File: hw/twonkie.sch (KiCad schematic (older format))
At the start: 54 parts, among them J1 USB_C_Plug, J2 USB_C_Receptacle, J3 USB_B_Micro, Q1 BSD840N, Q2 BSD840N, Q3 BSD840N, SW1 TACT, U1 AD8620, U2 AD8620, U3 AD8620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

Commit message: Half a PCB - USB-C side laid out
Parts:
- removed NT1: Net-Tie_2, symbol Device:Net-Tie_2
- added C9: 100n, Capacitor_SMD:C_0402_1005Metric_Pad0.74x0.62mm_HandSolder, symbol Device:C
- C1, C2, C3, C8: footprint (none) -> Capacitor_SMD:C_0402_1005Metric_Pad0.74x0.62mm_HandSolder
- C4: renamed from C6; footprint (none) -> Capacitor_SMD:C_0402_1005Metric_Pad0.74x0.62mm_HandSolder
- C5: renamed from C4; footprint (none) -> Capacitor_SMD:C_0402_1005Metric_Pad0.74x0.62mm_HandSolder
- C6: renamed from C7; footprint (none) -> Capacitor_SMD:C_0402_1005Metric_Pad0.74x0.62mm_HandSolder
- C7: renamed from C5; footprint (none) -> Capacitor_SMD:C_0402_1005Metric_Pad0.74x0.62mm_HandSolder
- DS1, DS2: footprint (none) -> LED_SMD:LED_Cree-PLCC4_3.2x2.8mm_CCW
- FB1: renamed from FB2; footprint (none) -> Inductor_SMD:L_0402_1005Metric_Pad0.77x0.64mm_HandSolder
- FB2: renamed from FB1; footprint (none) -> Inductor_SMD:L_0402_1005Metric_Pad0.77x0.64mm_HandSolder
- J1: footprint (none) -> twonkie:JAE_DX07P024AJ1R1500; symbol Connector:USB_C_Plug -> twonkie:USB_C_Plug
- J2: footprint (none) -> twonkie:EDAC_690-024-294T331_EdgeMount; symbol Connector:USB_C_Receptacle -> twonkie:USB_C_Receptacle
- J3: footprint (none) -> Connector_USB:USB_Micro-B_Wuerth_629105150521_CircularHoles
- R1, R14, R15, R16, R17, R18, R19, R2, R20, R21, R22, R23, R3: footprint (none) -> Resistor_SMD:R_0402_1005Metric_Pad0.72x0.64mm_HandSolder
- R10: renamed from R7; footprint (none) -> Resistor_SMD:R_0402_1005Metric_Pad0.72x0.64mm_HandSolder
- R11: renamed from R8; footprint (none) -> Resistor_SMD:R_0402_1005Metric_Pad0.72x0.64mm_HandSolder
- R12: renamed from R10; footprint (none) -> Resistor_SMD:R_0402_1005Metric_Pad0.72x0.64mm_HandSolder
- R13: renamed from R11; footprint (none) -> Resistor_SMD:R_0402_1005Metric_Pad0.72x0.64mm_HandSolder
- R4: renamed from R5; footprint (none) -> Resistor_SMD:R_0402_1005Metric_Pad0.72x0.64mm_HandSolder
- R5: renamed from R9; footprint (none) -> Resistor_SMD:R_0402_1005Metric_Pad0.72x0.64mm_HandSolder
- R6: renamed from R12; footprint (none) -> Resistor_SMD:R_0402_1005Metric_Pad0.72x0.64mm_HandSolder
- R7: renamed from R13; footprint (none) -> Resistor_SMD:R_0402_1005Metric_Pad0.72x0.64mm_HandSolder
- R8: renamed from R4; footprint (none) -> Resistor_SMD:R_0402_1005Metric_Pad0.72x0.64mm_HandSolder
- R9: renamed from R6; footprint (none) -> Resistor_SMD:R_0402_1005Metric_Pad0.72x0.64mm_HandSolder
- SW1: footprint (none) -> Button_Switch_SMD:SW_SPST_Omron_B3FS-100xP
- TP1, TP2, TP3, TP4, TP5: footprint (none) -> TestPoint:TestPoint_Pad_D1.5mm
- U1, U2: value AD8620 -> INA260; footprint (none) -> Package_SO:TSSOP-16_4.4x5mm_P0.65mm
- U3: value AD8620 -> MIC5504; footprint (none) -> Package_TO_SOT_SMD:SOT-23-5_HandSoldering
- U4: footprint (none) -> Package_QFP:LQFP-48_7x7mm_P0.5mm
- U5: footprint (none) -> Package_SO:MSOP-8_3x3mm_P0.65mm
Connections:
- net labels added: CC2_PLUG, RX1+, RX1-, RX2+, RX2-, SBU1, SBU2, TX1+, TX1-, TX2+, TX2-, TX_CLK, USBC_D+, USBC_D-, USB_B_D+, USB_B_D-, VBUS_PLUG, VBUS_RECEP
- net labels removed: TX_CLKIN, TX_CLKOUT, USB_B_DM, USB_B_DP
- wire segments 204 -> 203
- no-connect marks 5 -> 8
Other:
- note removed: "This space for rent"
- moved on the sheet: U1, U2

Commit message: Ratsnest Zero \o/
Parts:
- SW1: footprint Button_Switch_SMD:SW_SPST_Omron_B3FS-100xP -> Button_Switch_SMD:SW_SPST_EVQP7C; symbol Switch:SW_MEC_5E -> Switch:SW_Push
- TP1, TP2, TP3, TP4, TP5: footprint TestPoint:TestPoint_Pad_D1.5mm -> TestPoint:TestPoint_Pad_D1.0mm
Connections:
- net PB10 is gone; now on net LED_G_L: U4.21 (PB10)
- net PB12 is gone; now on net CC2_RPUSB: U4.25 (PB12)
- net PC13 is gone; now on net CC2_TX_EN: U4.2 (PC13)
- net BOOT: now also SW1.2; no longer SW1.3 (K), SW1.4 (A)
- net CC1_RA: now also U4.39 (PB3); no longer U4.29 (PA8)
- net CC1_RD: now also U4.40 (PB4); no longer U4.41 (PB5)
- net CC1_RP1A5: now also U4.45 (PB8); no longer U4.37 (PA14)
- net CC1_RP3A0: now also U4.41 (PB5); no longer U4.38 (PA15)
- net CC1_RPUSB: now also U4.3 (PC14); no longer U4.34 (PA13)
- net CC1_TX_DATA: now also U4.38 (PA15); no longer U4.40 (PB4)
- net CC1_TX_EN: now also U4.37 (PA14); no longer U4.19 (PB1)
- net CC2_RA: now also U4.34 (PA13); no longer U4.28 (PB15)
- net CC2_RD: now also U4.29 (PA8); no longer U4.45 (PB8)
- net CC2_RP1A5: now also U4.26 (PB13); no longer U4.3 (PC14)
- net CC2_RP3A0: now also U4.28 (PB15); no longer U4.4 (PC15)
- net CC2_RPUSB: no longer U4.18 (PB0)
- net CC2_TX_DATA: now also U4.4 (PC15); no longer U4.16 (PA6)
- net CC2_TX_EN: no longer U4.39 (PB3)
- net GND: no longer SW1.2
- net LED_G_L: no longer U4.22 (PB11)
- net LED_R_L: now also U4.22 (PB11); no longer U4.26 (PB13)
- no-connect marks 8 -> 5
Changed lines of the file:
@@
 $EndComp
 $Comp
-L Switch:SW_MEC_5E SW1
+L Switch:SW_Push SW1
 U 1 1 5FAB092D
-P 7700 3300
-F 0 "SW1" H 7700 3685 50  0000 C CNN
-F 1 "TACT" H 7700 3594 50  0000 C CNN
-F 2 "Button_Switch_SMD:SW_SPST_Omron_B3FS-100xP" H 7700 3600 50  0001 C CNN
-F 3 "http://www.apem.com/int/index.php?controller=attachment&id_attachment=1371" H 7700 3600 50  0001 C CNN
-	1    7700 3300
+P 7500 3200
+F 0 "SW1" H 7500 3400 50  0000 C CNN
+F 1 "TACT" H 7500 3100 50  0000 C CNN
+F 2 "Button_Switch_SMD:SW_SPST_EVQP7C" H 7500 3500 50  0001 C CNN
+F 3 "http://www.apem.com/int/index.php?controller=attachment&id_attachment=1371" H 7500 3500 50  0001 C CNN
+	1    7500 3200
 	-1   0    0    -1
 $EndComp
@@
 Wire Wire Line
 	7500 4850 8400 4850
-Text Label 7500 4550 0    50   ~ 0
+Text Label 7500 5750 0    50   ~ 0
 CC2_RPUSB
-Text Label 7500 4650 0    50   ~ 0
+Text Label 10500 5950 2    50   ~ 0
 CC1_TX_EN
 Text Label 7500 4750 0    50   ~ 0
 VBUS_ALERT_L
-Text Label 7500 4850 0    50   ~ 0
+Text Label 7500 4150 0    50   ~ 0
 CC2_TX_EN
 Wire Wire Line
@@
 Wire Wire Line
 	7500 5250 8400 5250
+Text Label 10500 6050 2    50   ~ 0
+CC1_TX_DATA
 Text Label 7500 4950 0    50   ~ 0
-CC1_TX_DATA
-Text Label 7500 5050 0    50   ~ 0
 CC1_RD
 Text Label 7500 5150 0    50   ~ 0
@@
 Wire Wire Line
 	7500 5650 8400 5650
-Text Label 7500 5350 0    50   ~ 0
+Text Label 10500 5350 2    50   ~ 0
 CC2_RD
 Text Label 7500 5450 0    50   ~ 0
 TX_CLK
 Text Label 7500 5650 0    50   ~ 0
-LED_G_L
+LED_R_L
 Wire Wire Line
 	7500 5850 8400 5850
@@
 Wire Wire Line
 	7500 6050 8400 6050
-Text Label 7500 5850 0    50   ~ 0
-LED_R_L
 Text Label 7500 5950 0    50   ~ 0
 LED_B_L
-Text Label 7500 6050 0    50   ~ 0
+Text Label 10500 5850 2    50   ~ 0
 CC2_RA
 Wire Wire Line
@@
 Text Label 10500 5050 2    50   ~ 0
 TX_CLK
-Text Label 10500 5150 2    50   ~ 0
+Text Label 7500 4350 0    50   ~ 0
 CC2_TX_DATA
 Text Label 10500 5250 2    50   ~ 0
@@
 Wire Wire Line
 	10500 5650 9600 5650
-Text Label 10500 5350 2    50   ~ 0
+Text Label 7500 4850 0    50   ~ 0
 CC1_RA
 Text Label 10500 5450 2    50   ~ 0
@@
 Text Label 10500 5750 2    50   ~ 0
 USB_B_D+
-Text Label 10500 5850 2    50   ~ 0
-CC1_RPUSB
-Text Label 10500 5950 2    50   ~ 0
+Text Label 7500 5350 0    50   ~ 0
 CC1_RP1A5
-Text Label 10500 6050 2    50   ~ 0
+Text Label 7500 5050 0    50   ~ 0
 CC1_RP3A0
 Wire Wire Line
@@
 F 0 "TP5" V 7500 3800 50  0000 C CNN
 F 1 "TestPoint" V 7604 3622 50  0001 C CNN
-F 2 "TestPoint:TestPoint_Pad_D1.5mm" H 7700 3550 50  0001 C CNN
+F 2 "TestPoint:TestPoint_Pad_D1.0mm" H 7700 3550 50  0001 C CNN
 F 3 "~" H 7700 3550 50  0001 C CNN
 	1    7500 3550
 	0    -1   -1   0
 $EndComp
-Wire Wire Line
-	7500 3300 7500 3200
-Connection ~ 7500 3200
-Wire Wire Line
-	7900 3300 7900 3200
 $Comp
 L power:GND #PWR0124
 U 1 1 5FE51FD2
-P 7900 3300
-F 0 "#PWR0124" H 7900 3050 50  0001 C CNN
-F 1 "GND" H 7905 3127 50  0000 C CNN
-F 2 "" H 7900 3300 50  0001 C CNN
-F 3 "" H 7900 3300 50  0001 C CNN
-	1    7900 3300
+P 7700 3200
+F 0 "#PWR0124" H 7700 2950 50  0001 C CNN
+F 1 "GND" H 7705 3027 50  0000 C CNN
+F 2 "" H 7700 3200 50  0001 C CNN
+F 3 "" H 7700 3200 50  0001 C CNN
+	1    7700 3200
 	-1   0    0    -1
 $EndComp
-Connection ~ 7900 3300
 Wire Wire Line
 	7100 3950 8400 3950
 Wire Wire Line
-	7500 3200 7100 3200
+	7300 3200 7100 3200
 $Comp
 L power:+3V3 #PWR0125
@@
 F 0 "TP1" V 7500 4000 50  0000 C CNN
 F 1 "TestPoint" V 7604 3822 50  0001 C CNN
-F 2 "TestPoint:TestPoint_Pad_D1.5mm" H 7700 3750 50  0001 C CNN
+F 2 "TestPoint:TestPoint_Pad_D1.0mm" H 7700 3750 50  0001 C CNN
 F 3 "~" H 7700 3750 50  0001 C CNN
 	1    7500 3750
@@
 F 0 "TP2" V 7500 4100 50  0000 C CNN
 F 1 "TestPoint" V 7604 3922 50  0001 C CNN
-F 2 "TestPoint:TestPoint_Pad_D1.5mm" H 7700 3850 50  0001 C CNN
+F 2 "TestPoint:TestPoint_Pad_D1.0mm" H 7700 3850 50  0001 C CNN
 F 3 "~" H 7700 3850 50  0001 C CNN
 	1    7500 3850
@@
 Wire Wire Line
 	8400 4150 7500 4150
-Text Label 7500 4250 0    50   ~ 0
-CC2_RP1A5
-Text Label 7500 4350 0    50   ~ 0
+Text Label 7500 6050 0    50   ~ 0
 CC2_RP3A0
 Wire Wire Line
@@
 Wire Wire Line
 	8400 5750 7500 5750
-Text Label 7500 5750 0    50   ~ 0
-PB12
 Text Label 7500 5550 0    50   ~ 0
-PB10
-Text Label 7500 4150 0    50   ~ 0
-PC13
+LED_G_L
 $Comp
 L Connector:TestPoint TP3
@@
 F 0 "TP3" V 10500 5700 50  0000 C CNN
 F 1 "TestPoint" V 10604 5522 50  0001 C CNN
-F 2 "TestPoint:TestPoint_Pad_D1.5mm" H 10700 5450 50  0001 C CNN
+F 2 "TestPoint:TestPoint_Pad_D1.0mm" H 10700 5450 50  0001 C CNN
 F 3 "~" H 10700 5450 50  0001 C CNN
 	1    10500 5450
@@
 F 0 "TP4" V 10500 5800 50  0000 C CNN
 F 1 "TestPoint" V 10604 5622 50  0001 C CNN
-F 2 "TestPoint:TestPoint_Pad_D1.5mm" H 10700 5550 50  0001 C CNN
+F 2 "TestPoint:TestPoint_Pad_D1.0mm" H 10700 5550 50  0001 C CNN
 F 3 "~" H 10700 5550 50  0001 C CNN
 	1    10500 5550
@@
 	-1   0    0    1
 $EndComp
-NoConn ~ 7500 4150
-NoConn ~ 7500 5550
-NoConn ~ 7500 5750
 NoConn ~ 10500 4950
 NoConn ~ 4600 7300
@@
 	1    0    0    -1
 $EndComp
+Text Label 7500 5850 0    50   ~ 0
+CC2_RP1A5
+Text Label 7500 4250 0    50   ~ 0
+CC1_RPUSB
 $EndSCHEMATC

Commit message: Silk screen, ground plane fixes, move vias out of pads, part numbers
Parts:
- C1, C5: DigiKey P/N (none) -> 1276-1235-1-ND; Manufacturer (none) -> Samsung Electro-Mechanics; Mfg P/N (none) -> CL05A105MQ5NNNC
- C2, C7: DigiKey P/N (none) -> 1276-1481-1-ND; Manufacturer (none) -> Samsung Electro-Mechanics; Mfg P/N (none) -> CL05A475KQ5NRNC
- C3, C4, C8, C9: DigiKey P/N (none) -> 1276-6720-1-ND; Manufacturer (none) -> Samsung Electro-Mechanics; Mfg P/N (none) -> CL05B104KA5NNNC
- C6: DigiKey P/N (none) -> 1276-1028-1-ND; Manufacturer (none) -> Samsung Electro-Mechanics; Mfg P/N (none) -> CL05B103KB5NNNC
- D1: DigiKey P/N (none) -> BZT52C5V6-13-FDICT-ND; Manufacturer (none) -> Diodes Inc.; Mfg P/N (none) -> BZT52C5V6-13-F
- DS1, DS2: value LED_ARBG -> CLVBA-FKA; symbol Device:LED_ARBG -> Device:LED_RABG; DigiKey P/N (none) -> CLVBA-FKA-CAEDH8BBB7A363CT-ND; Manufacturer (none) -> Cree; Mfg P/N (none) -> CLVBA-FKA-CAEDH8BBB7A363
- FB1, FB2: DigiKey P/N (none) -> 490-1006-1-ND; Manufacturer (none) -> MuRata; Mfg P/N (none) -> BLM15AG601SN1D
- J1: value USB_C_Plug -> DX07P024AJ1R1500; DigiKey P/N (none) -> 670-2868-1-ND; Manufacturer (none) -> JAE; Mfg P/N (none) -> DX07P024AJ1R1500
- J2: value USB_C_Receptacle -> 690-024-294T331; DigiKey P/N (none) -> 151-1601-1-ND; Manufacturer (none) -> EDAC; Mfg P/N (none) -> 690-024-294T331
- J3: value USB_B_Micro -> 629105150521; DigiKey P/N (none) -> 732-5960-1-ND; Manufacturer (none) -> Würth; Mfg P/N (none) -> 629105150521
- Q1, Q2, Q3: DigiKey P/N (none) -> BSD840NH6327XTSA1CT-ND; Manufacturer (none) -> Infineon; Mfg P/N (none) -> BSD840NH6327XTSA1
- R1: DigiKey P/N (none) -> 311-51.1KLRCT-ND; Manufacturer (none) -> Yageo; Mfg P/N (none) -> RC0402FR-0751K1L
- R10, R18: Manufacturer (none) -> Yageo; Mfg P/N (none) -> RC0402FR-071KL
- R11, R19: Manufacturer (none) -> Yageo; Mfg P/N (none) -> RC0402FR-0712K1L
- R12, R20: Manufacturer (none) -> Yageo; Mfg P/N (none) -> RC0402FR-075K11L
- R13, R21: Manufacturer (none) -> Yageo; Mfg P/N (none) -> RC0402FR-0735K7L
- R14, R22: Manufacturer (none) -> Yageo; Mfg P/N (none) -> RC0402FR-07200RL
- R15, R23: Manufacturer (none) -> Yageo; Mfg P/N (none) -> RC0402FR-07100RL
- R16, R8: DigiKey P/N (none) -> 311-301KLRCT-ND; Manufacturer (none) -> Yageo; Mfg P/N (none) -> RC0402FR-07301KL
- R17, R9: DigiKey P/N (none) -> 311-4.75KLCT-ND; Manufacturer (none) -> Yageo; Mfg P/N (none) -> RC0402FR-074K75L
- R2, R5: DigiKey P/N (none) -> YAG3239CT-ND; Manufacturer (none) -> Yageo; Mfg P/N (none) -> RC0402FR-07806RL
- R3, R6: DigiKey P/N (none) -> YAG3189CT-ND; Manufacturer (none) -> Yageo; Mfg P/N (none) -> RC0402FR-07576RL
- R4, R7: DigiKey P/N (none) -> YAG3199CT-ND; Manufacturer (none) -> Yageo; Mfg P/N (none) -> RC0402FR-07604RL
- SW1: value TACT -> EVQ-P7M01P; DigiKey P/N (none) -> P16770CT-ND; Manufacturer (none) -> Panasonic; Mfg P/N (none) -> EVQ-P7M01P
- TP1, TP2, TP3, TP4, TP5: DigiKey P/N (none) -> -; Manufacturer (none) -> -; Mfg P/N (none) -> -
- U1, U2: DigiKey P/N (none) -> 296-47777-1-ND; Manufacturer (none) -> TI; Mfg P/N (none) -> INA260AIPWR
- U3: DigiKey P/N (none) -> 576-4764-1-ND; Manufacturer (none) -> Microchip; Mfg P/N (none) -> MIC5504-3.3YM5-TR
- U4: DigiKey P/N (none) -> 497-19319-1-ND; Manufacturer (none) -> STMicro; Mfg P/N (none) -> STM32F042C6T6TR
- U5: DigiKey P/N (none) -> AD8606ARMZREELCT-ND; Manufacturer (none) -> Analog Devices; Mfg P/N (none) -> AD8606ARMZ-REEL
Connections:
- net +5V: now also DS1.2 (A), DS2.2 (A); no longer DS1.1 (A), DS2.1 (A)
- net CC1_RA: now also U4.45 (PB8); no longer U4.39 (PB3)
- net CC1_RD: now also U4.39 (PB3); no longer U4.40 (PB4)
- net CC1_RP1A5: now also U4.41 (PB5); no longer U4.45 (PB8)
- net CC1_RP3A0: now also U4.3 (PC14); no longer U4.41 (PB5)
- net CC1_RPUSB: now also U4.40 (PB4); no longer U4.3 (PC14)
- net CC2_RA: now also U4.29 (PA8); no longer U4.34 (PA13)
- net CC2_RD: now also U4.26 (PB13); no longer U4.29 (PA8)
- net CC2_RP1A5: now also U4.28 (PB15); no longer U4.26 (PB13)
- net CC2_RP3A0: now also U4.34 (PA13); no longer U4.28 (PB15)
- net at R2.1: now also DS1.1 (RK); no longer DS1.2 (RK)
- net at R5.1: now also DS2.1 (RK); no longer DS2.2 (RK)
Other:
- moved on the sheet: DS2, R5, R6, R7

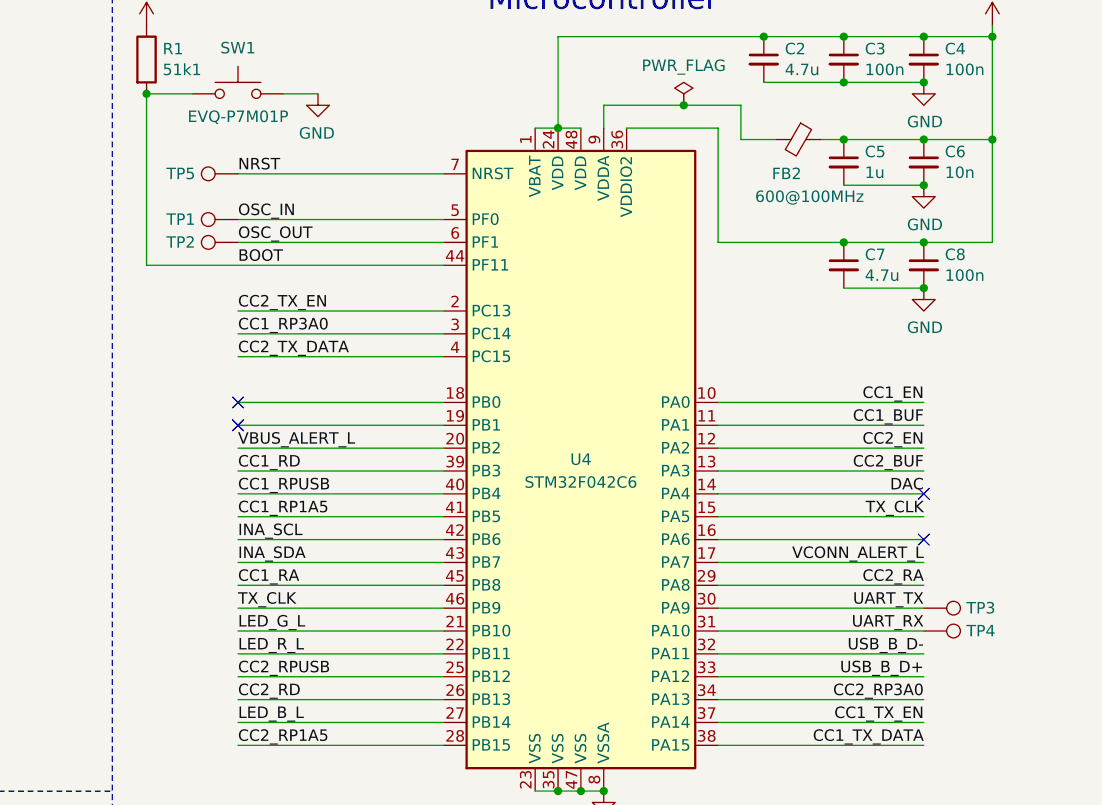
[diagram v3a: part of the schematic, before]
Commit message: Switch uC to combo LQFP+QFN footprint, re-route most connections
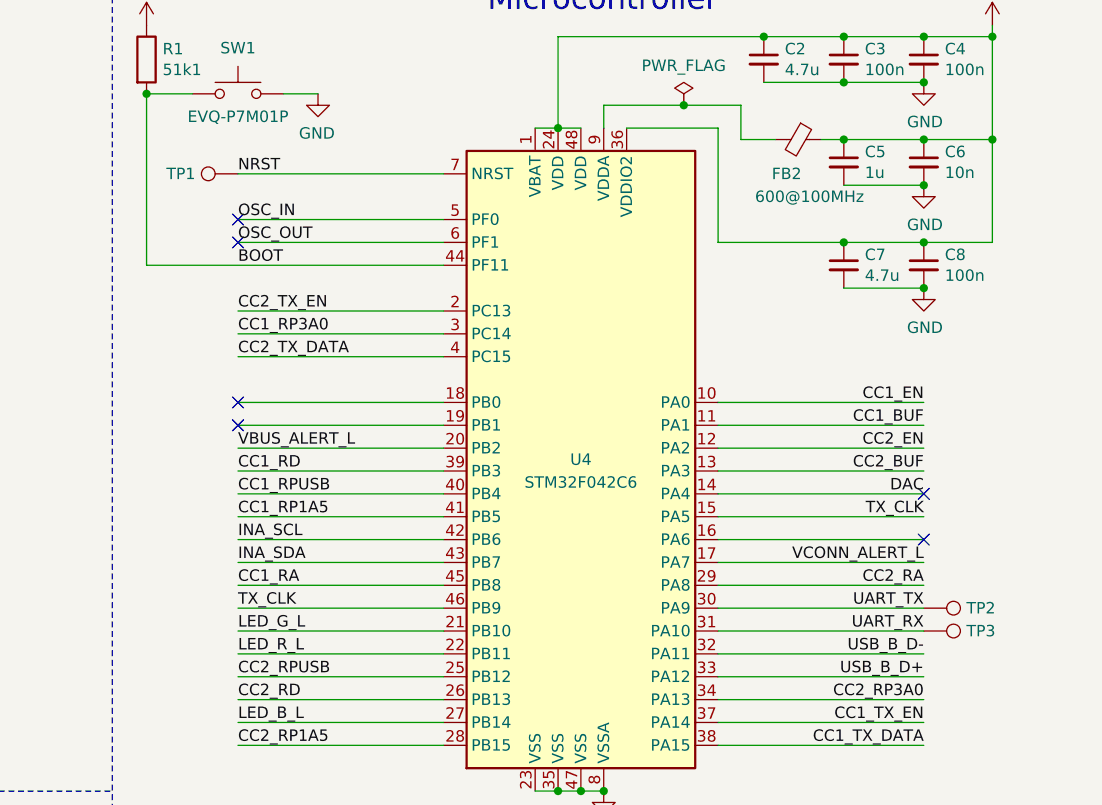
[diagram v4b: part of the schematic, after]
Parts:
- removed TP1, TP2: TestPoint, TestPoint:TestPoint_Pad_D1.0mm, symbol Connector:TestPoint
- renumbered TP5 to TP1, TP3 to TP2, TP4 to TP3
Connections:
- no-connect marks 5 -> 7
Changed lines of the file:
@@
 NRST
 $Comp
-L Connector:TestPoint TP5
+L Connector:TestPoint TP1
 U 1 1 5FE22EC0
 P 7500 3550
-F 0 "TP5" V 7500 3800 50  0000 C CNN
+F 0 "TP1" V 7500 3800 50  0000 C CNN
 F 1 "TestPoint" V 7604 3622 50  0001 C CNN
 F 2 "TestPoint:TestPoint_Pad_D1.0mm" H 7700 3550 50  0001 C CNN
@@
 	1    0    0    -1
 $EndComp
-$Comp
-L Connector:TestPoint TP1
-U 1 1 5FE60C7A
-P 7500 3750
-F 0 "TP1" V 7500 4000 50  0000 C CNN
-F 1 "TestPoint" V 7604 3822 50  0001 C CNN
-F 2 "TestPoint:TestPoint_Pad_D1.0mm" H 7700 3750 50  0001 C CNN
-F 3 "~" H 7700 3750 50  0001 C CNN
-F 4 "-" H 7500 3750 50  0001 C CNN "DigiKey P/N"
-F 5 "-" H 7500 3750 50  0001 C CNN "Manufacturer"
-F 6 "-" H 7500 3750 50  0001 C CNN "Mfg P/N"
-	1    7500 3750
-	0    -1   -1   0
-$EndComp
-$Comp
-L Connector:TestPoint TP2
-U 1 1 5FE60F1E
-P 7500 3850
-F 0 "TP2" V 7500 4100 50  0000 C CNN
-F 1 "TestPoint" V 7604 3922 50  0001 C CNN
-F 2 "TestPoint:TestPoint_Pad_D1.0mm" H 7700 3850 50  0001 C CNN
-F 3 "~" H 7700 3850 50  0001 C CNN
-F 4 "-" H 7500 3850 50  0001 C CNN "DigiKey P/N"
-F 5 "-" H 7500 3850 50  0001 C CNN "Manufacturer"
-F 6 "-" H 7500 3850 50  0001 C CNN "Mfg P/N"
-	1    7500 3850
-	0    -1   -1   0
-$EndComp
 Wire Wire Line
 	8400 4350 7500 4350
@@
 LED_G_L
 $Comp
-L Connector:TestPoint TP3
+L Connector:TestPoint TP2
 U 1 1 5FEEE9C1
 P 10500 5450
-F 0 "TP3" V 10500 5700 50  0000 C CNN
+F 0 "TP2" V 10500 5700 50  0000 C CNN
 F 1 "TestPoint" V 10604 5522 50  0001 C CNN
 F 2 "TestPoint:TestPoint_Pad_D1.0mm" H 10700 5450 50  0001 C CNN
@@
 $EndComp
 $Comp
-L Connector:TestPoint TP4
+L Connector:TestPoint TP3
 U 1 1 5FEEFA7D
 P 10500 5550
-F 0 "TP4" V 10500 5800 50  0000 C CNN
+F 0 "TP3" V 10500 5800 50  0000 C CNN
 F 1 "TestPoint" V 10604 5622 50  0001 C CNN
 F 2 "TestPoint:TestPoint_Pad_D1.0mm" H 10700 5550 50  0001 C CNN
@@
 Wire Wire Line
 	7700 3200 7850 3200
+NoConn ~ 7500 3750
+NoConn ~ 7500 3850
 $EndSCHEMATC
